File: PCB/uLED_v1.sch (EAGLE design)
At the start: 17 parts, among them IC1 ATSAMD21E, J2 455-1750-1-ND, SW1 EG1218, U1 AP2112K-3.3

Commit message: Saturday Morning Commit
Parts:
- removed RESET: (no value), microbuilder:SWITCH_TACT_SMT4.6X2.8
- removed SW1: EG1218, microbuilder:SWITCH_DPDTEG1390
- removed U$3: 20MM_BATTERY, mikes:20MM_BATTERY
- added BT1: (no value), SparkFun-Batteries:BATTERY-12MM_SMD
- added J3, J4, J5, J6: (no value), SparkFun-Connectors:CONN_01
- J2: value 455-1750-1-ND -> (none); device SparkFun-Connectors:CONN_03 -> SparkFun-Connectors:CONN_01
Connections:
- net N$2 renamed BLUELED
- net N$3 renamed GREENLED
- removed net N$1: J1.1, R1.2
- removed net SERCOM_1+3.0: IC1.PA16/I2C/I0/SERCOM1+3.0
- removed net SERCOM_1+3.1: IC1.PA17/I2C/I1/SERCOM1+3.1
- removed net VOUT: C1.1, SW1.P1, U1.EN, U1.IN
- new net REDLED: IC1.PA15/I15/SERCOM3+4.3, J1.1, R1.2
- net 3.3V: now also J6.1
- net GND: now also BT1.-, J2.1; no longer RESET.S, RESET.S1, U$3.-
- net RESETN: now also J3.1; no longer J2.1, RESET.P, RESET.P1
- net SCDIO: now also J5.1; no longer J2.3
- net SWCLK: now also J4.1; no longer J2.2
- net VBAT: now also BT1.+; no longer U$3.+2
- net VHIGH: now also C1.1, U1.EN, U1.IN; no longer SW1.O1

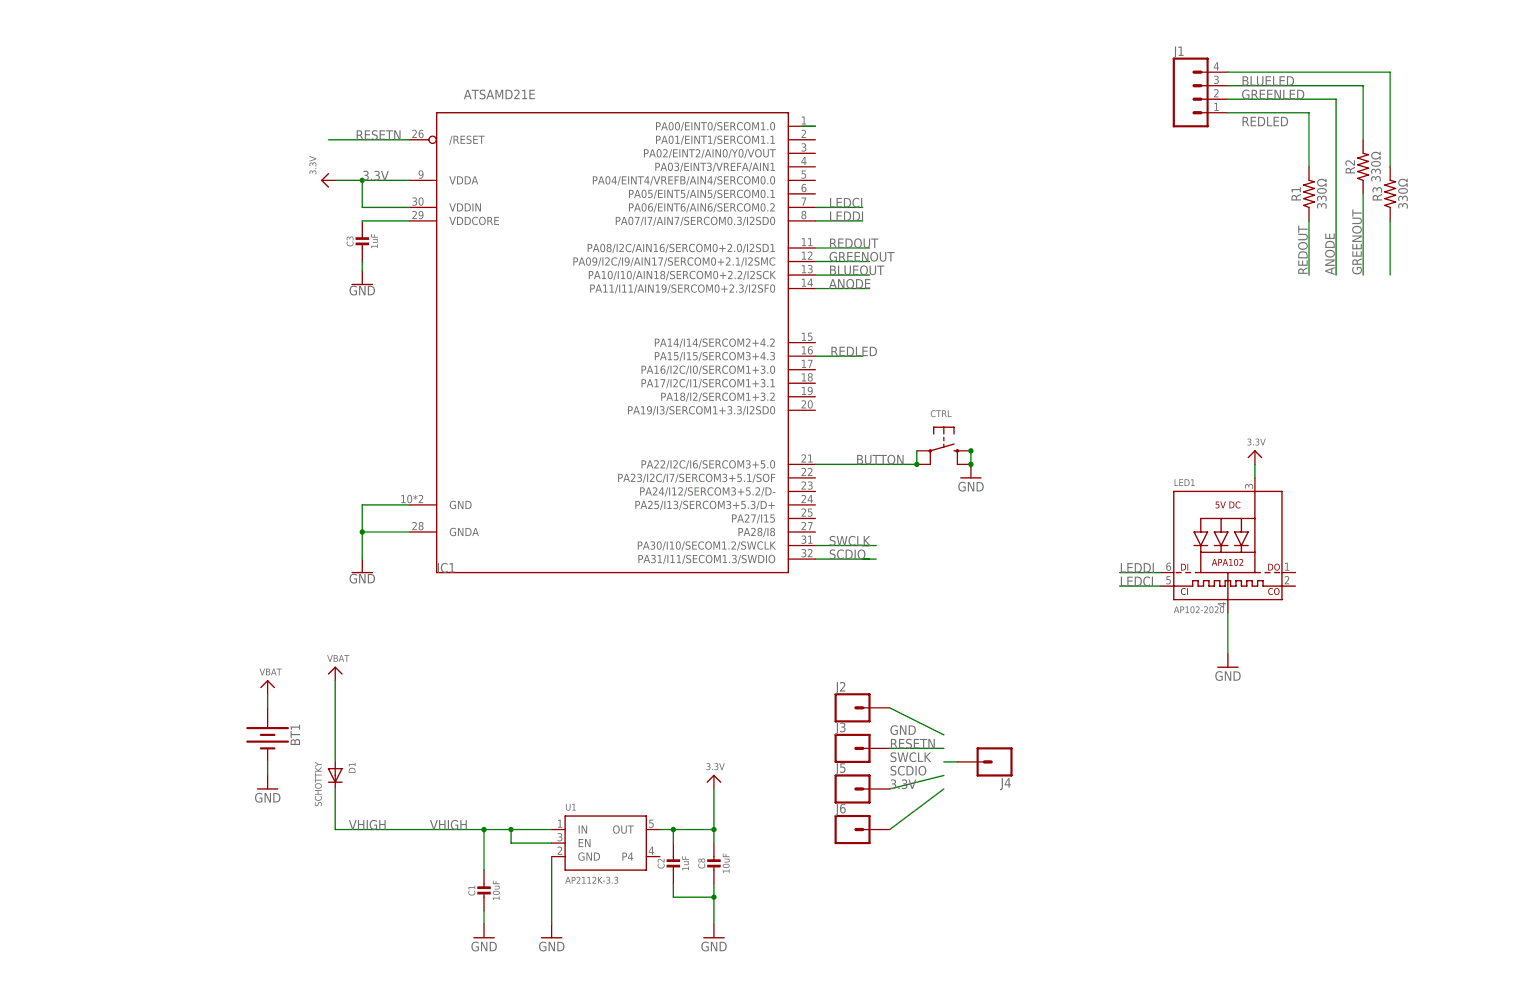
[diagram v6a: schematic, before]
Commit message: Adding new PCB 16mm
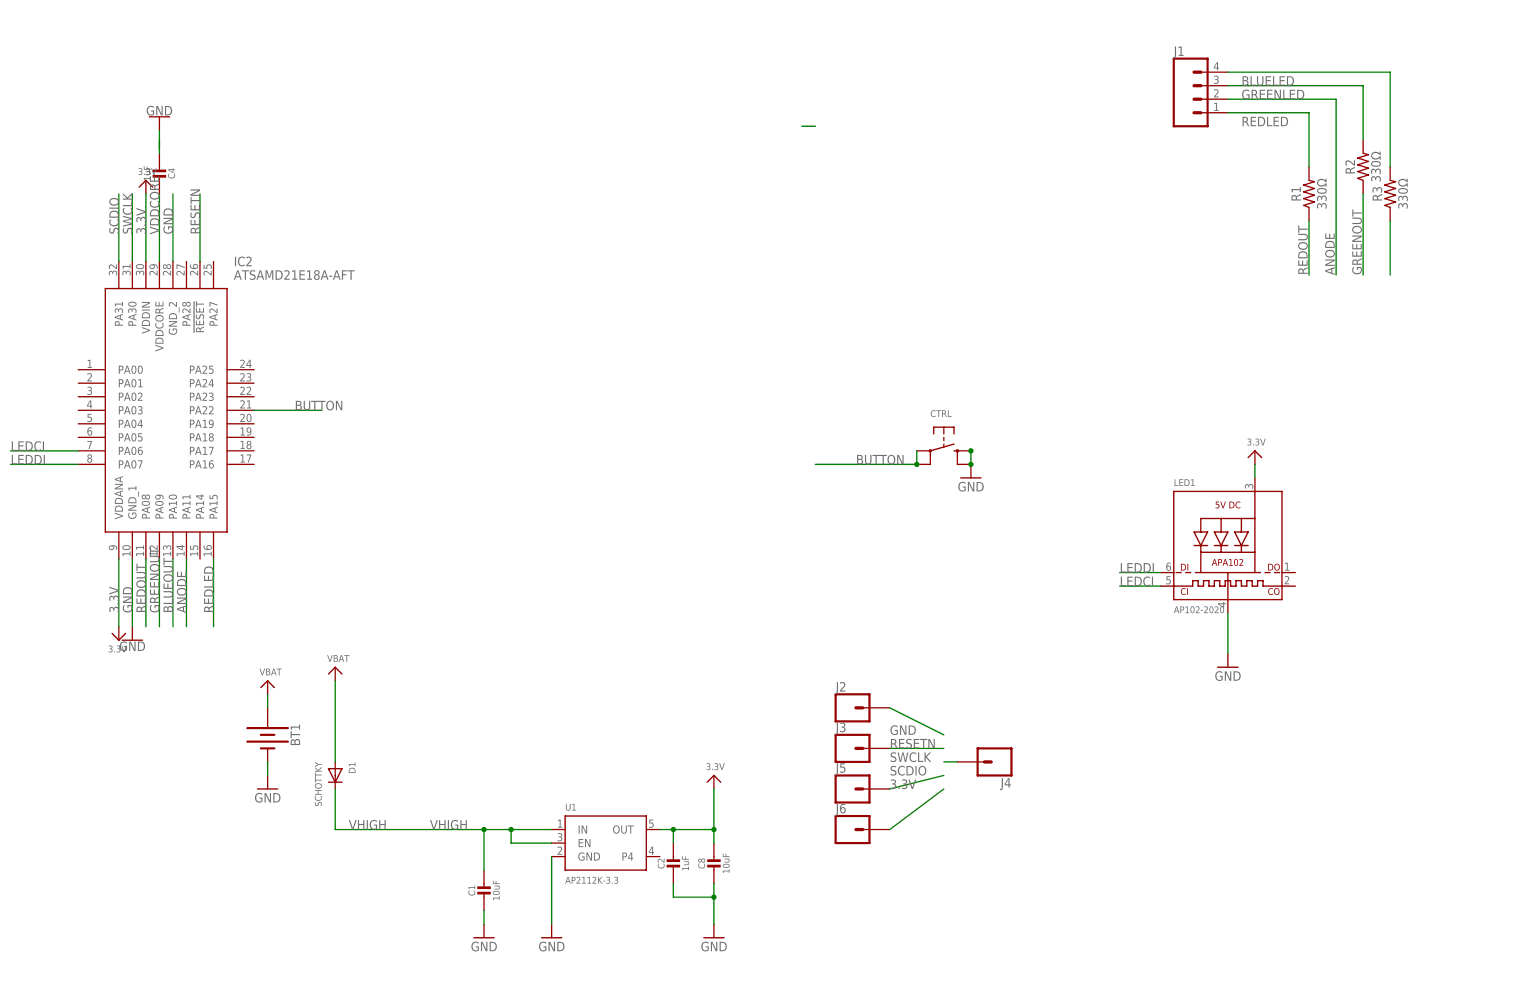
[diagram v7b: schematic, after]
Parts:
- removed C3: 1uF, microbuilder:CAP_CERAMIC0603_NO
- removed IC1: ATSAMD21E, microbuilder:ATSAMD21E
- added C4: 1uF, microbuilder:CAP_CERAMIC0603_NO
- added IC2: ATSAMD21E18A-AFT, SamacSys_Parts:ATSAMD21E18A-AFT
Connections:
- removed net D3: IC1.PA00/EINT0/SERCOM1.0
- net 3.3V: now also IC2.VDDANA, IC2.VDDIN; no longer IC1.VDDA, IC1.VDDIN
- net ANODE: now also IC2.PA11; no longer IC1.PA11/I11/AIN19/SERCOM0+2.3/I2SF0
- net BLUEOUT: now also IC2.PA10; no longer IC1.PA10/I10/AIN18/SERCOM0+2.2/I2SCK
- net BUTTON: now also IC2.PA22; no longer IC1.PA22/I2C/I6/SERCOM3+5.0
- net GND: now also C4.2, IC2.GND_1, IC2.GND_2; no longer C3.2, IC1.GND, IC1.GNDA
- net GREENOUT: now also IC2.PA09; no longer IC1.PA09/I2C/I9/AIN17/SERCOM0+2.1/I2SMC
- net LEDCI: now also IC2.PA06; no longer IC1.PA06/EINT6/AIN6/SERCOM0.2
- net LEDDI: now also IC2.PA07; no longer IC1.PA07/I7/AIN7/SERCOM0.3/I2SD0
- net REDLED: now also IC2.PA15; no longer IC1.PA15/I15/SERCOM3+4.3
- net REDOUT: now also IC2.PA08; no longer IC1.PA08/I2C/AIN16/SERCOM0+2.0/I2SD1
- net RESETN: now also IC2.!RESET; no longer IC1./RESET
- net SCDIO: now also IC2.PA31; no longer IC1.PA31/I11/SECOM1.3/SWDIO
- net SWCLK: now also IC2.PA30; no longer IC1.PA30/I10/SECOM1.2/SWCLK
- net VDDCORE: now also C4.1, IC2.VDDCORE; no longer C3.1, IC1.VDDCORE
